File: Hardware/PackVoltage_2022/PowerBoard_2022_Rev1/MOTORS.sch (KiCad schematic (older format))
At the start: 70 parts, among them Q15 BUK7M8R5-40HX, Q16 BUK7M8R5-40HX, Q17 BUK7M8R5-40HX, Q18 BUK7M8R5-40HX, Q19 BUK7M8R5-40HX, Q20 BUK7M8R5-40HX, Q21 BUK7M8R5-40HX, U40 LT1910, U41 LT1910, U42 LT1910, U43 LT1910, U44 INA281, U45 INA281, U46 INA281, U47 INA281, U48 LT1910, U49 LT1910, U50 LT1910, U51 INA281, U52 INA281, U53 INA281

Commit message: Made it to layout, found out about gnd via
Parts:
- renumbered C68 to C71, C69 to C72, C70 to C73, C71 to C74, C72 to C75, C73 to C76, C74 to C77, C75 to C78, C76 to C79, C77 to C80, C78 to C81, C79 to C82, C80 to C83, C81 to C84, D28 to D25, D29 to D26, D30 to D27, D31 to D28, D32 to D29, D33 to D30, D34 to D31, F20 to F10, F21 to F11, F22 to F12, F23 to F13, F24 to F14, F18 to F8, F19 to F9, Q15 to Q3, Q16 to Q4, Q17 to Q5, Q18 to Q6, Q19 to Q7, Q20 to Q8, Q21 to Q9, R1 to R27, R55 to R28, R56 to R29, R57 to R30, R58 to R31, R59 to R32, R60 to R33, R61 to R34, R62 to R35, R63 to R36, R64 to R37, R65 to R38, R66 to R39, R67 to R40, R68 to R41, R69 to R42, R70 to R43, R71 to R44, R72 to R45, R73 to R46, R74 to R47, U40 to U25, U41 to U26, U42 to U27, U43 to U28, U44 to U29, U45 to U30, U46 to U31, U47 to U32, U48 to U33, U49 to U34, U50 to U35, U51 to U36, U52 to U37, U53 to U38

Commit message: fixed Fuses
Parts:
- F10, F11, F12, F13, F14, F8, F9: footprint Fuse:Fuse_0603_1608Metric_Pad1.05x0.95mm_HandSolder -> MRDT_Passives:ATC_Fuse_Block
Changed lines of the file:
@@
 F 0 "F8" V 2550 950 50  0000 L CNN
 F 1 "20" V 2700 950 50  0000 L CNN
-F 2 "Fuse:Fuse_0603_1608Metric_Pad1.05x0.95mm_HandSolder" V 2630 1000 50  0001 C CNN
+F 2 "MRDT_Passives:ATC_Fuse_Block" V 2630 1000 50  0001 C CNN
 F 3 "~" H 2700 1000 50  0001 C CNN
 	1    2700 1000
@@
 F 0 "F12" V 7700 1050 50  0000 L CNN
 F 1 "20" V 7850 1050 50  0000 L CNN
-F 2 "Fuse:Fuse_0603_1608Metric_Pad1.05x0.95mm_HandSolder" V 7780 1100 50  0001 C CNN
+F 2 "MRDT_Passives:ATC_Fuse_Block" V 7780 1100 50  0001 C CNN
 F 3 "~" H 7850 1100 50  0001 C CNN
 	1    7850 1100
@@
 F 0 "F9" V 2650 2650 50  0000 L CNN
 F 1 "20" V 2800 2650 50  0000 L CNN
-F 2 "Fuse:Fuse_0603_1608Metric_Pad1.05x0.95mm_HandSolder" V 2730 2700 50  0001 C CNN
+F 2 "MRDT_Passives:ATC_Fuse_Block" V 2730 2700 50  0001 C CNN
 F 3 "~" H 2800 2700 50  0001 C CNN
 	1    2800 2700
@@
 F 0 "F13" V 7750 2700 50  0000 L CNN
 F 1 "20" V 7900 2700 50  0000 L CNN
-F 2 "Fuse:Fuse_0603_1608Metric_Pad1.05x0.95mm_HandSolder" V 7830 2750 50  0001 C CNN
+F 2 "MRDT_Passives:ATC_Fuse_Block" V 7830 2750 50  0001 C CNN
 F 3 "~" H 7900 2750 50  0001 C CNN
 	1    7900 2750
@@
 F 0 "F10" V 2650 4300 50  0000 L CNN
 F 1 "20" V 2800 4300 50  0000 L CNN
-F 2 "Fuse:Fuse_0603_1608Metric_Pad1.05x0.95mm_HandSolder" V 2730 4350 50  0001 C CNN
+F 2 "MRDT_Passives:ATC_Fuse_Block" V 2730 4350 50  0001 C CNN
 F 3 "~" H 2800 4350 50  0001 C CNN
 	1    2800 4350
@@
 F 0 "F14" V 7800 4700 50  0000 L CNN
 F 1 "20" V 7950 4700 50  0000 L CNN
-F 2 "Fuse:Fuse_0603_1608Metric_Pad1.05x0.95mm_HandSolder" V 7880 4750 50  0001 C CNN
+F 2 "MRDT_Passives:ATC_Fuse_Block" V 7880 4750 50  0001 C CNN
 F 3 "~" H 7950 4750 50  0001 C CNN
 	1    7950 4750
@@
 F 0 "F11" V 3200 6200 50  0000 L CNN
 F 1 "20" V 3350 6200 50  0000 L CNN
-F 2 "Fuse:Fuse_0603_1608Metric_Pad1.05x0.95mm_HandSolder" V 3280 6250 50  0001 C CNN
+F 2 "MRDT_Passives:ATC_Fuse_Block" V 3280 6250 50  0001 C CNN
 F 3 "~" H 3350 6250 50  0001 C CNN
 	1    3350 6250

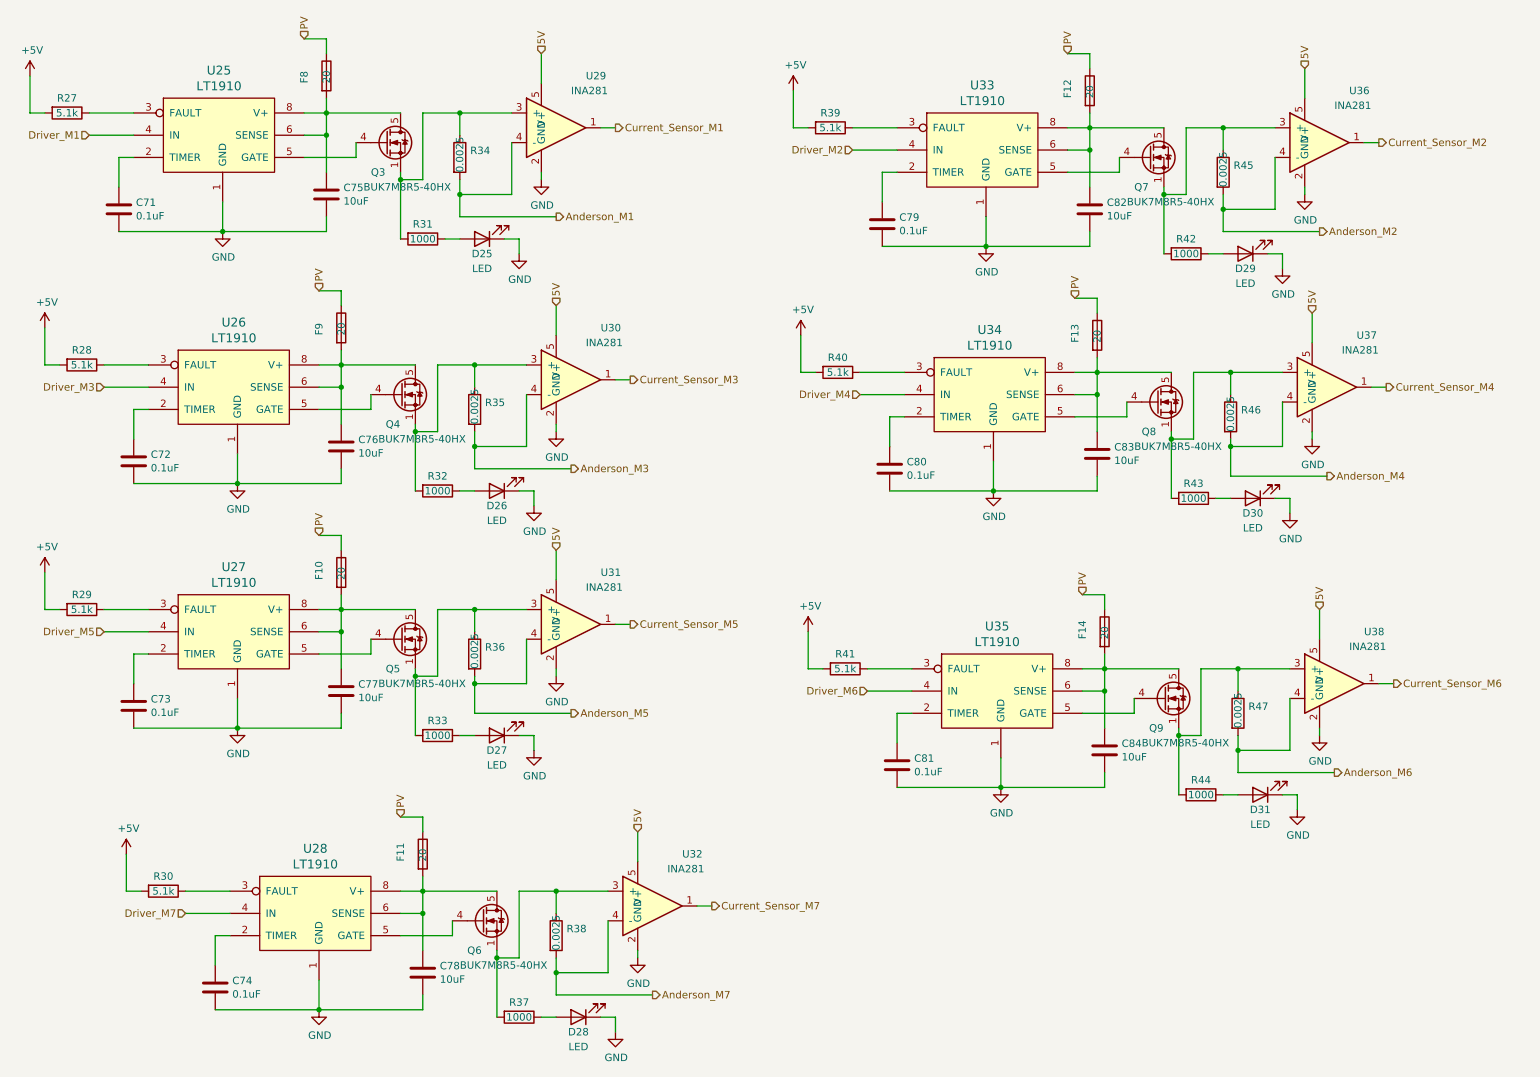
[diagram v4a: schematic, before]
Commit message: Organized  Stuff into groups and changed how we organize our board
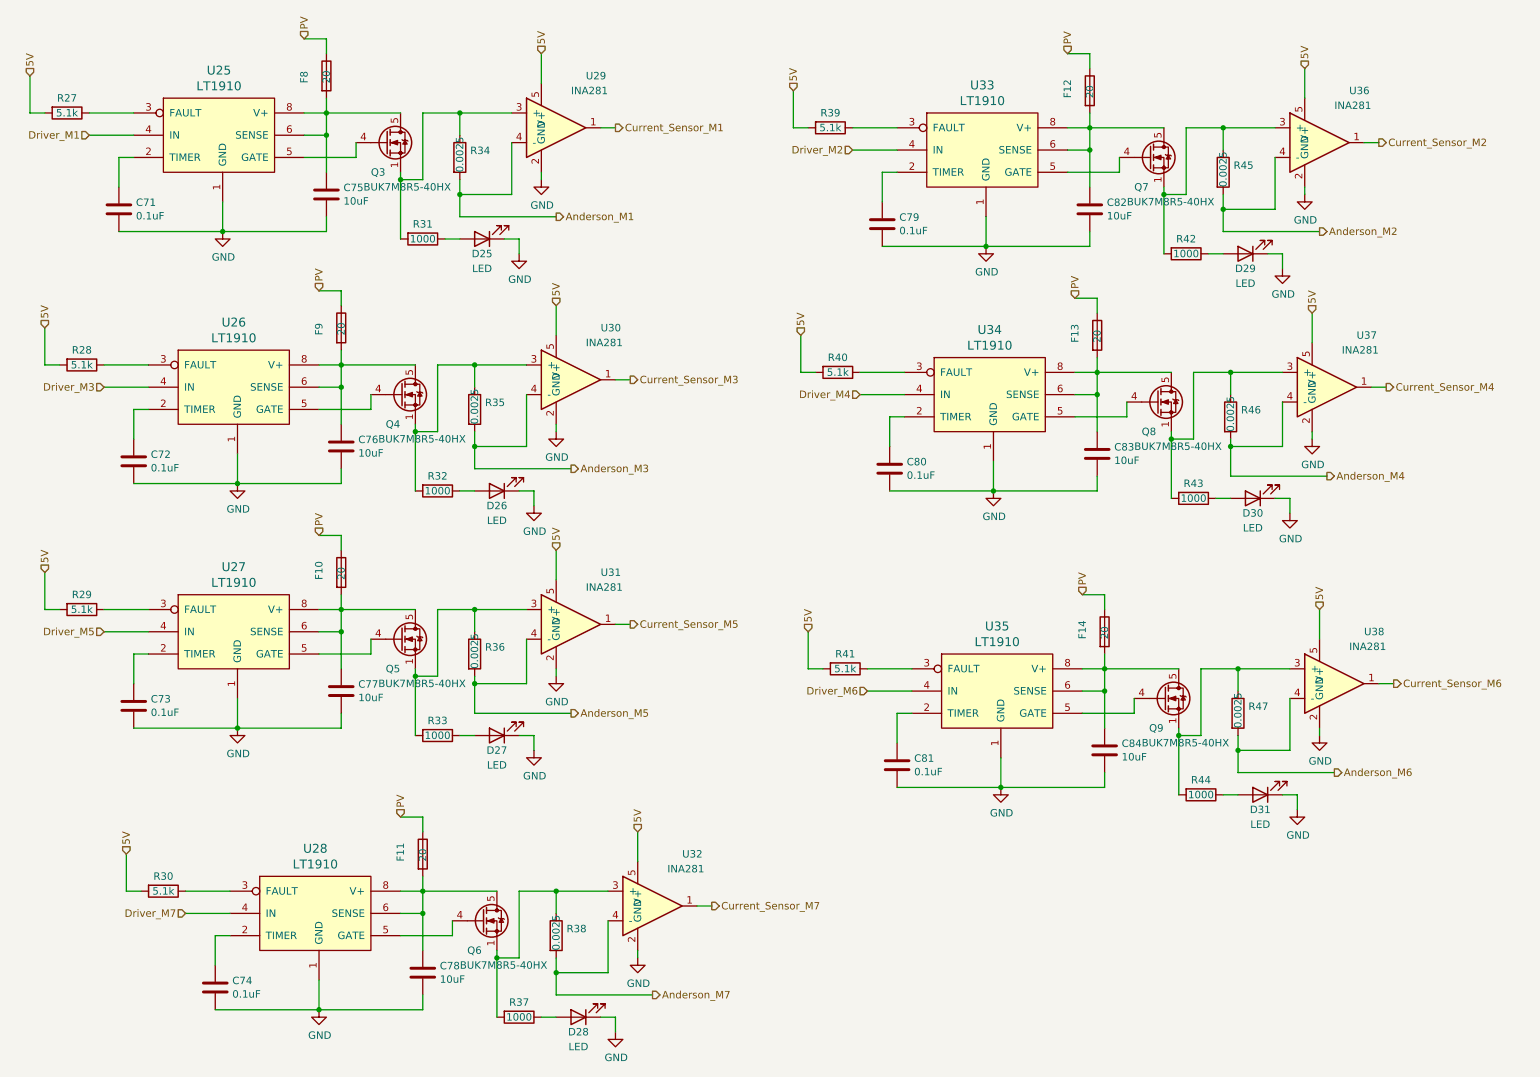
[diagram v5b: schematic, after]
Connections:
- net +5V is gone; now on net 5V: R27.2, R28.2, R29.2, R30.2, R39.2, R40.2, R41.2
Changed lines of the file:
@@
 EESchema Schematic File Version 4
-EELAYER 30 0
+LIBS:PowerBoard_2022_Rev1-cache
+EELAYER 26 0
 EELAYER END
 $Descr A4 11693 8268
@@
 Wire Wire Line
 	1100 1250 1400 1250
-$Comp
-L power:+5V #PWR054
-U 1 1 615D7F71
-P 700 1000
-F 0 "#PWR054" H 700 850 50  0001 C CNN
-F 1 "+5V" H 715 1173 50  0000 C CNN
-F 2 "" H 700 1000 50  0001 C CNN
-F 3 "" H 700 1000 50  0001 C CNN
-	1    700  1000
-	1    0    0    -1
-$EndComp
 Wire Wire Line
 	700  1000 700  1250
@@
 Wire Wire Line
 	6250 1350 6550 1350
-$Comp
-L power:+5V #PWR070
-U 1 1 616A0116
-P 5850 1100
-F 0 "#PWR070" H 5850 950 50  0001 C CNN
-F 1 "+5V" H 5865 1273 50  0000 C CNN
-F 2 "" H 5850 1100 50  0001 C CNN
-F 3 "" H 5850 1100 50  0001 C CNN
-	1    5850 1100
-	1    0    0    -1
-$EndComp
 Wire Wire Line
 	5850 1100 5850 1350
@@
 Wire Wire Line
 	1200 2950 1500 2950
-$Comp
-L power:+5V #PWR055
-U 1 1 616A8F90
-P 800 2700
-F 0 "#PWR055" H 800 2550 50  0001 C CNN
-F 1 "+5V" H 815 2873 50  0000 C CNN
-F 2 "" H 800 2700 50  0001 C CNN
-F 3 "" H 800 2700 50  0001 C CNN
-	1    800  2700
-	1    0    0    -1
-$EndComp
 Wire Wire Line
 	800  2700 800  2950
@@
 Wire Wire Line
 	6300 3000 6600 3000
-$Comp
-L power:+5V #PWR071
-U 1 1 616B4D54
-P 5900 2750
-F 0 "#PWR071" H 5900 2600 50  0001 C CNN
-F 1 "+5V" H 5915 2923 50  0000 C CNN
-F 2 "" H 5900 2750 50  0001 C CNN
-F 3 "" H 5900 2750 50  0001 C CNN
-	1    5900 2750
-	1    0    0    -1
-$EndComp
 Wire Wire Line
 	5900 2750 5900 3000
@@
 Wire Wire Line
 	1200 4600 1500 4600
-$Comp
-L power:+5V #PWR056
-U 1 1 616C39F4
-P 800 4350
-F 0 "#PWR056" H 800 4200 50  0001 C CNN
-F 1 "+5V" H 815 4523 50  0000 C CNN
-F 2 "" H 800 4350 50  0001 C CNN
-F 3 "" H 800 4350 50  0001 C CNN
-	1    800  4350
-	1    0    0    -1
-$EndComp
 Wire Wire Line
 	800  4350 800  4600
@@
 Wire Wire Line
 	6350 5000 6650 5000
-$Comp
-L power:+5V #PWR072
-U 1 1 616E7811
-P 5950 4750
-F 0 "#PWR072" H 5950 4600 50  0001 C CNN
-F 1 "+5V" H 5965 4923 50  0000 C CNN
-F 2 "" H 5950 4750 50  0001 C CNN
-F 3 "" H 5950 4750 50  0001 C CNN
-	1    5950 4750
-	1    0    0    -1
-$EndComp
 Wire Wire Line
 	5950 4750 5950 5000
@@
 Wire Wire Line
 	1350 6250 1350 6500
-$Comp
-L power:+5V #PWR057
-U 1 1 616D60E4
-P 1350 6250
-F 0 "#PWR057" H 1350 6100 50  0001 C CNN
-F 1 "+5V" H 1365 6423 50  0000 C CNN
-F 2 "" H 1350 6250 50  0001 C CNN
-F 3 "" H 1350 6250 50  0001 C CNN
-	1    1350 6250
-	1    0    0    -1
-$EndComp
 Wire Wire Line
 	1750 6500 2050 6500
@@
 	1    0    0    -1
 $EndComp
+Text HLabel 700  1000 1    50   Input ~ 0
+5V
+Text HLabel 800  2700 1    50   Input ~ 0
+5V
+Text HLabel 800  4350 1    50   Input ~ 0
+5V
+Text HLabel 1350 6250 1    50   Input ~ 0
+5V
+Text HLabel 5950 4750 1    50   Input ~ 0
+5V
+Text HLabel 5900 2750 1    50   Input ~ 0
+5V
+Text HLabel 5850 1100 1    50   Input ~ 0
+5V
 $EndSCHEMATC

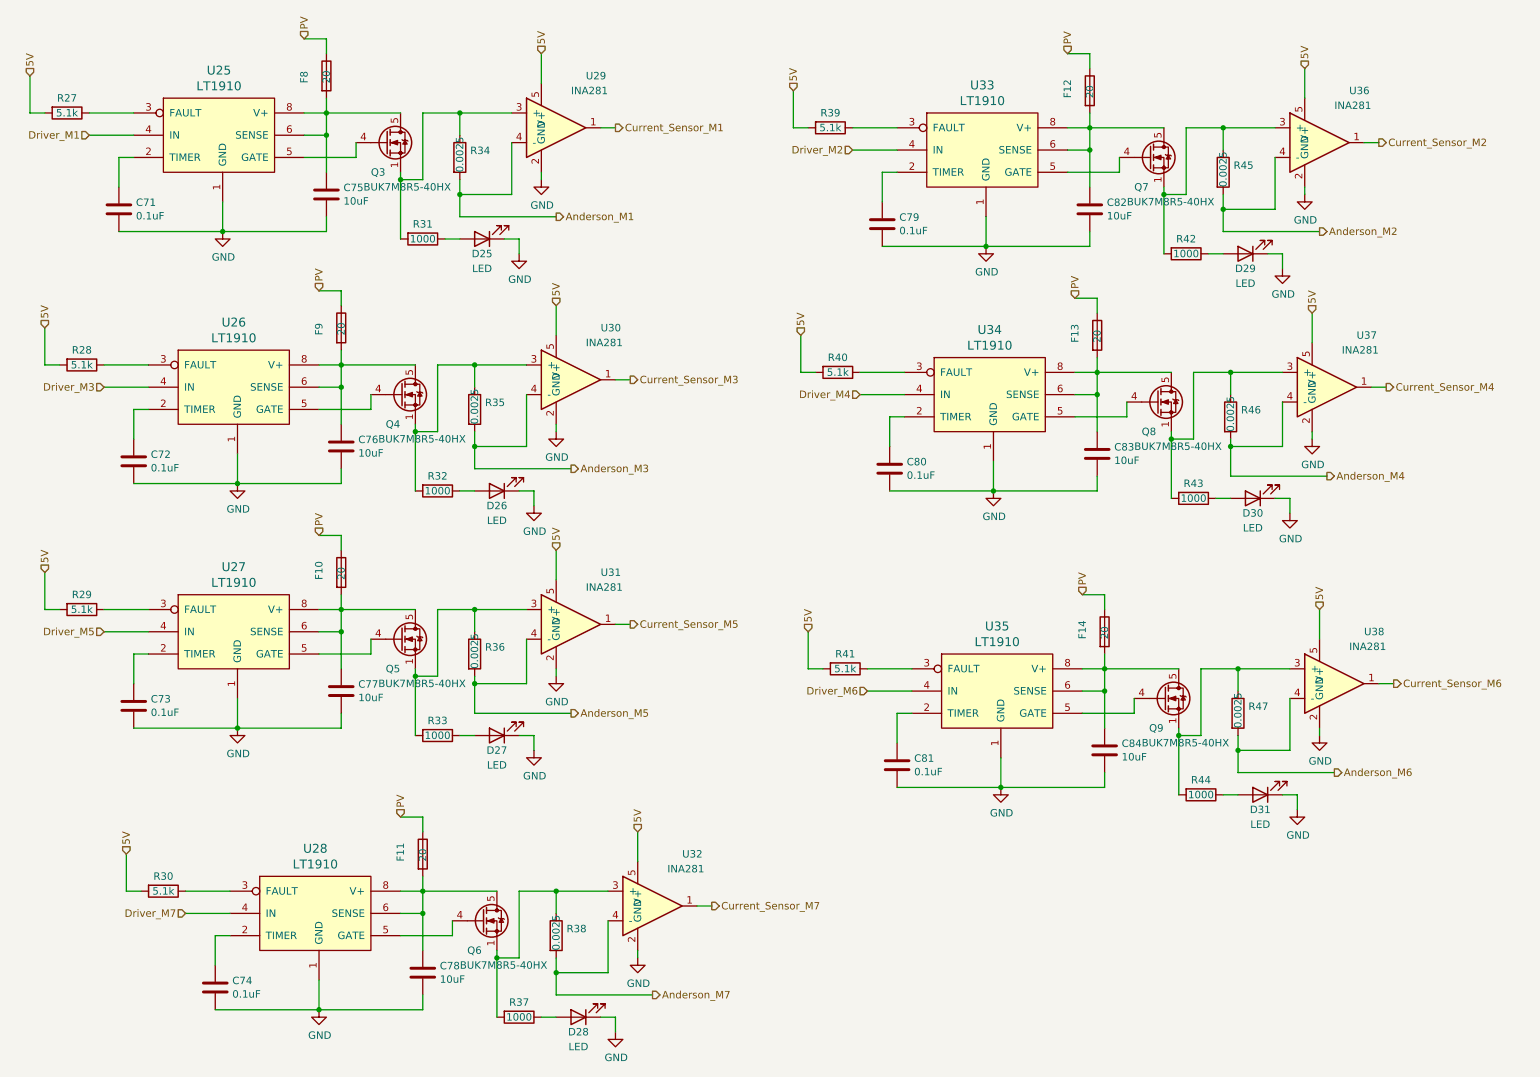
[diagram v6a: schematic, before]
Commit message: Removed redundant LED's in Actuation circuits and final touches on SciAct Layout
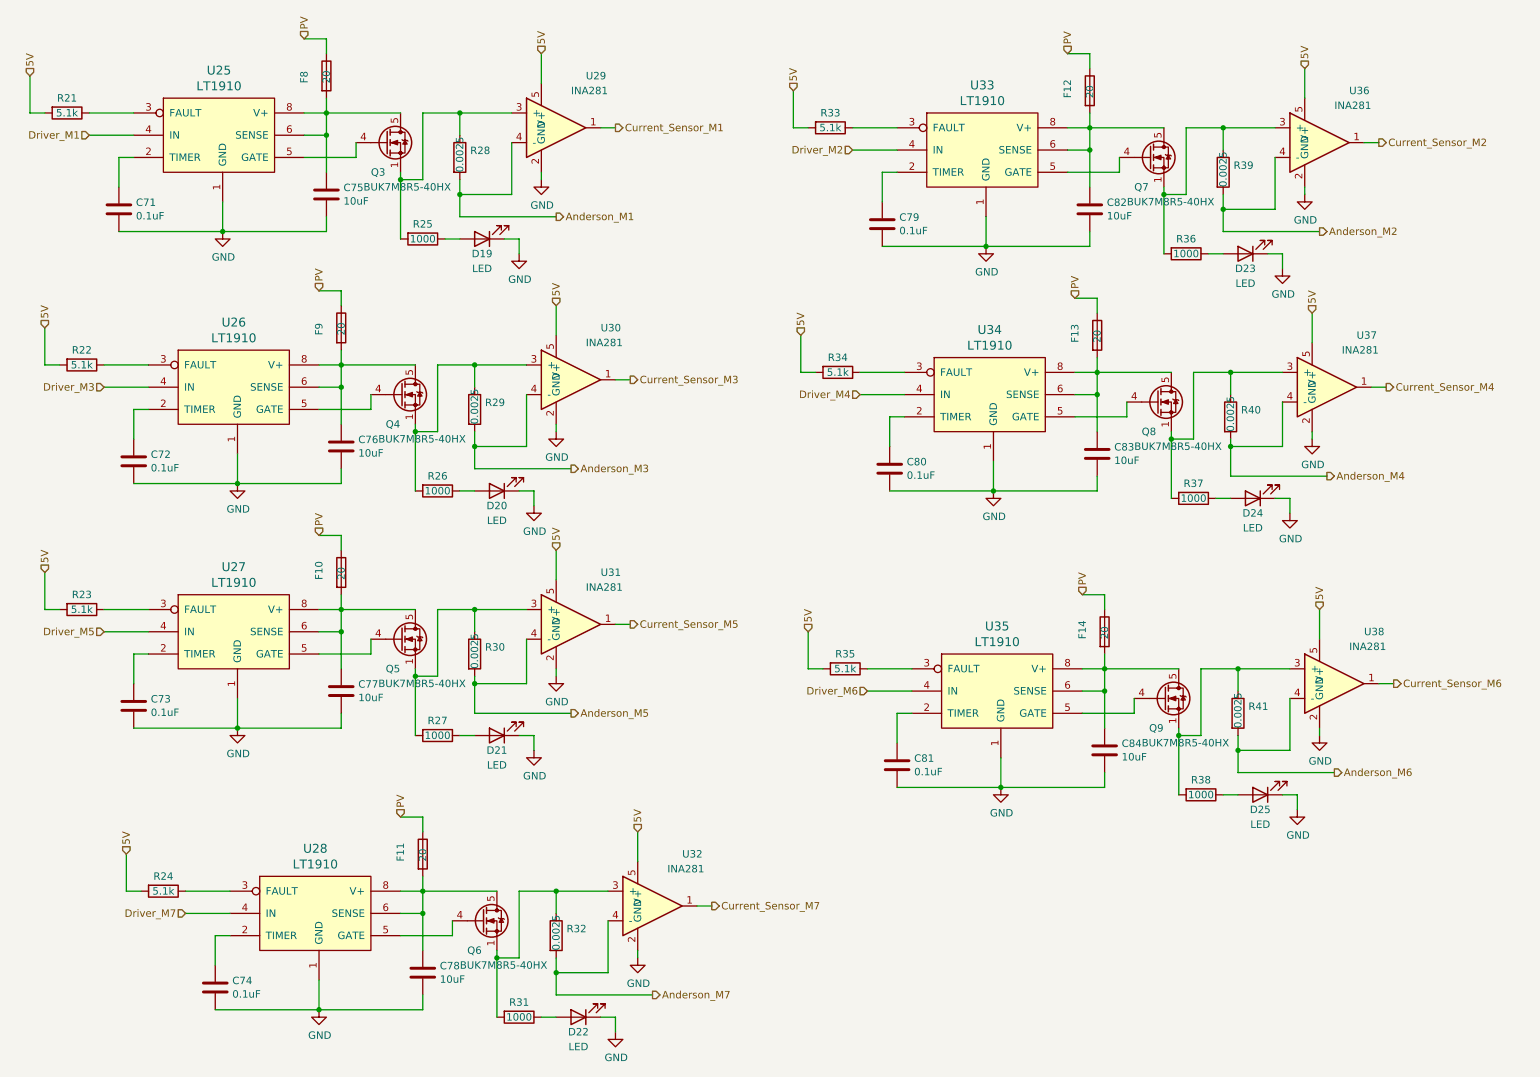
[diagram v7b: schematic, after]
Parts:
- renumbered D25 to D19, D26 to D20, D27 to D21, D28 to D22, D29 to D23, D30 to D24, D31 to D25, R27 to R21, R28 to R22, R29 to R23, R30 to R24, R31 to R25, R32 to R26, R33 to R27, R34 to R28, R35 to R29, R36 to R30, R37 to R31, R38 to R32, R39 to R33, R40 to R34, R41 to R35, R42 to R36, R43 to R37, R44 to R38, R45 to R39, R46 to R40, R47 to R41
